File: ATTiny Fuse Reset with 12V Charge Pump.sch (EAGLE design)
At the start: 70 parts, among them IC1 74HC04D, IC2 ATTinyx4, IC3 ATTinyx5/13, M1 MOUNTINGHOLE2.0, M2 MOUNTINGHOLE2.0, Q1 BSS138, Q2 PMV65XP, Q3 BSS138, Q4 BSS138, Q5 BSS138, Q6 BSS138, Q7 BSS138, Q8 BSS130, SW4 SWITCH_SPDT, SW5 SWITCH_SPDT, U1 ARDUINOR3-BPLACE

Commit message: Schematic and board layout improvment
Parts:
- LED1: value green -> pmode
- LED10: value yellow -> H.B.
- LED2: value red -> err
- LED3: value red -> PB5 rst
- LED4: value red -> PB4
- LED5: value red -> PB3
- LED6: value red -> PB2
- LED7: value red -> PB1
- LED8: value red -> PB0
- LED9: value green -> HV on
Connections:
- net N$7: now also A1.PB4; no longer IC1E.I
- net SCI: now also IC1C.I; no longer IC1A.I
- net SDI_MOSI: no longer IC1D.I
- net SII-MISO: now also IC1A.I; no longer IC1C.I

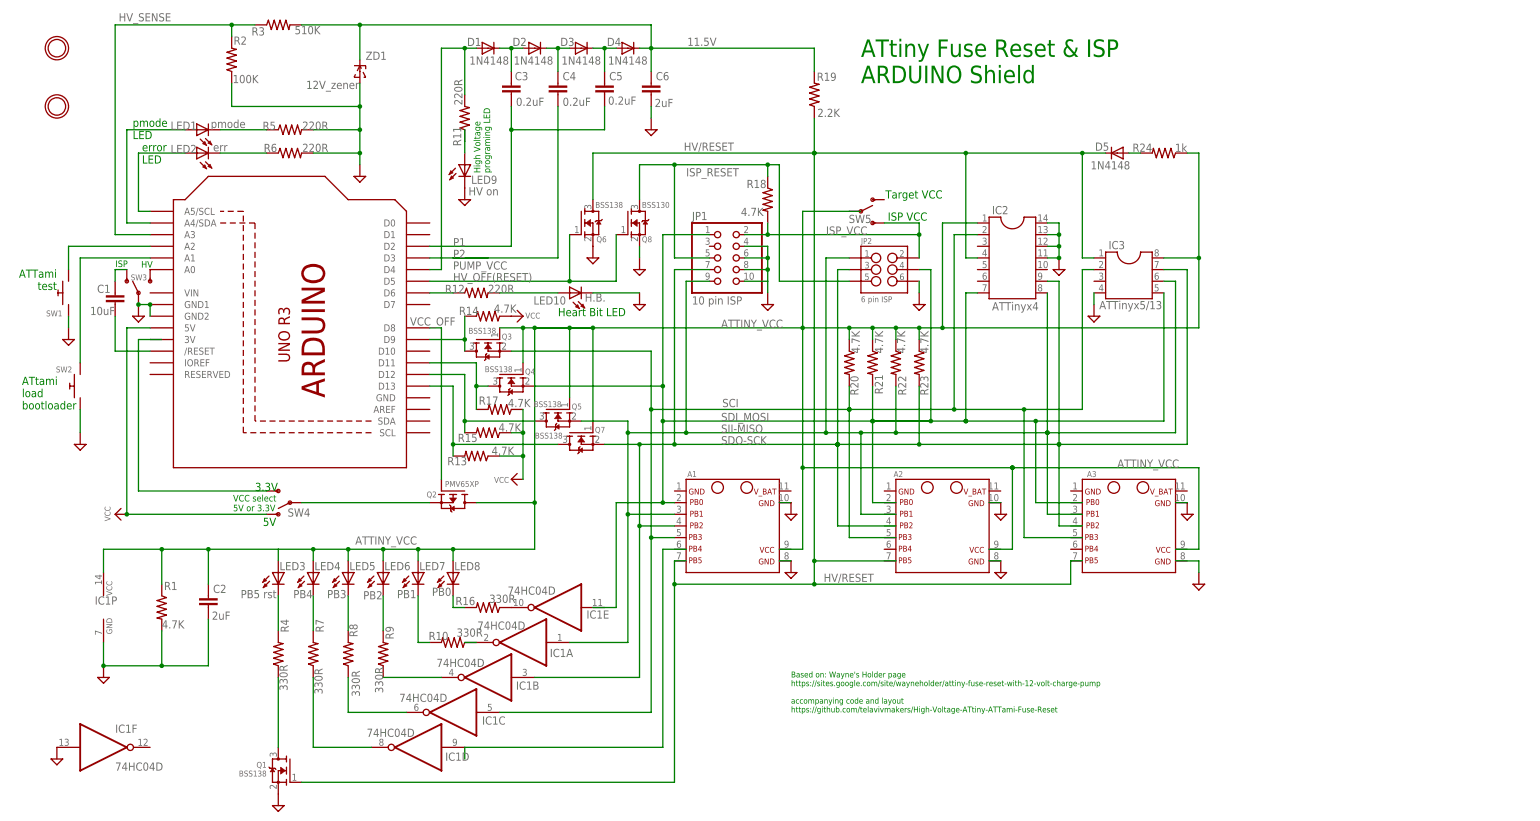
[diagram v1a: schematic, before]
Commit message: "TARGET/ ISP VCC switch"-B-Gone
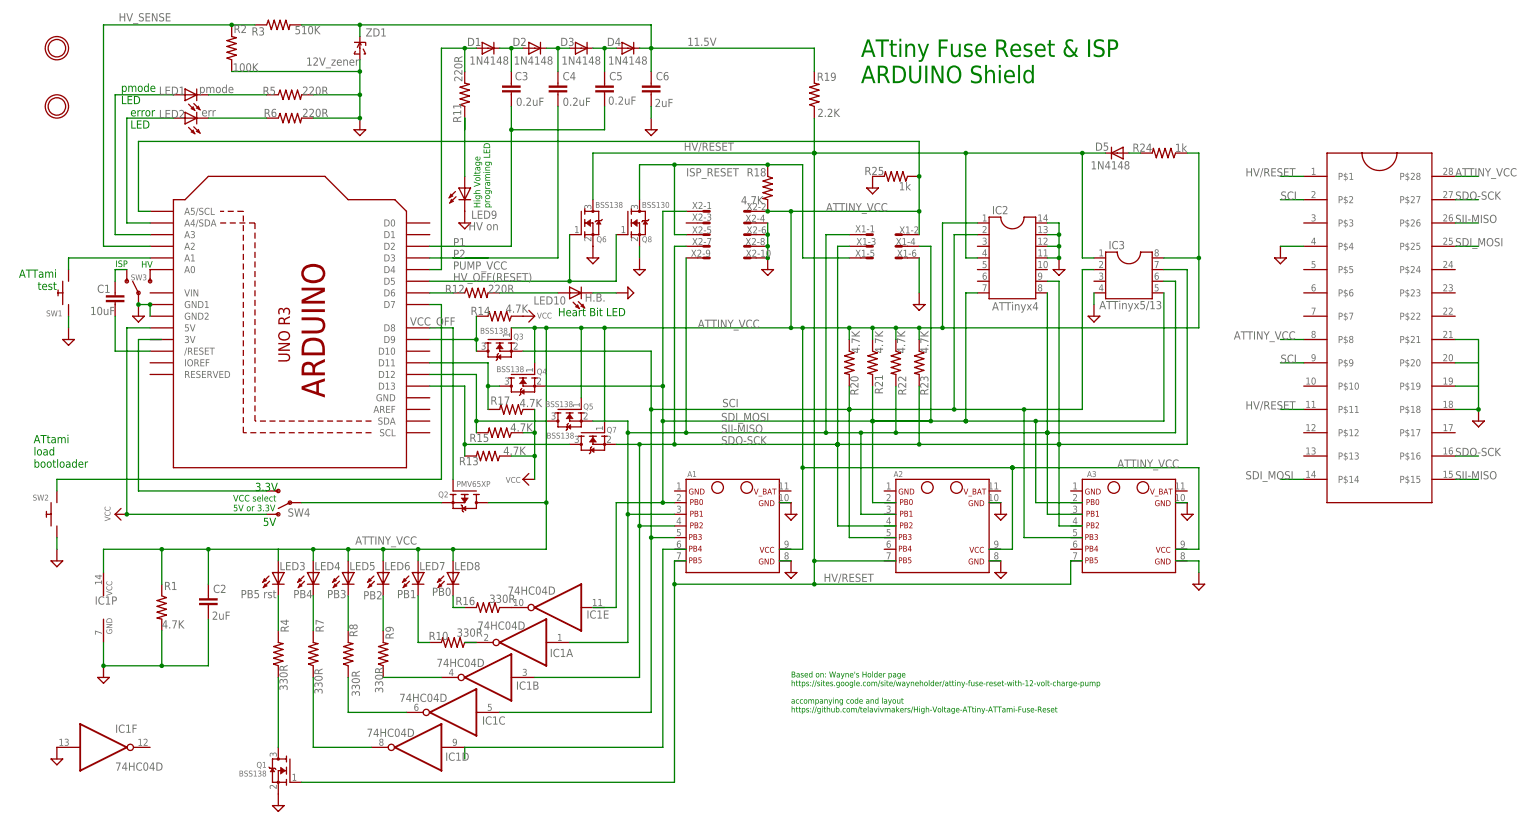
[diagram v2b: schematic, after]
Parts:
- removed JP1: 10 pin ISP, microbuilder:HEADER-2X5
- removed JP2: 6 pin ISP, SparkFun-Connectors:M03X2
- removed SW5: SWITCH_SPDT, SparkFun-Electromechanical:SWITCH_SPDT
- added R25: 1k, ATtami:RESISTOR0805-RES
- added U$1: ZIFSOCKET-28-3ZIFFSOCKET-28-3, SparkFun-Connectors:ZIFSOCKET-28-3ZIFFSOCKET-28-3
- added X1: 057-006-1, con-panduit:057-006-1
- added X2: 057-010-1, con-panduit:057-010-1
- IC2: device gm-ics:DIL14 -> ic-package:DIL14S
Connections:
- removed net ISP_VCC: JP1.2, JP2.2, R18.2, SW5.S
- new net N$50: U$1.P$20
- new net N$51: U$1.P$19
- net ATTINY_VCC: now also R18.2, R25.1, U$1.P$28, U$1.P$8, U1.A5/SCL, X1-2.S, X2-2.S; no longer SW5.P
- net GND: now also R25.2, U$1.P$18, U$1.P$21, U$1.P$4, X1-6.S, X2-10.S, X2-4.S, X2-6.S, X2-8.S; no longer JP1.10, JP1.4, JP1.6, JP1.8, JP2.6
- net HV/RESET: now also U$1.P$1, U$1.P$11
- net HV_SENSE: now also U1.A2; no longer U1.A3
- net ISP_RESET: now also X1-5.S, X2-5.S; no longer JP1.5, JP2.5
- net N$17: now also U1.A4/SDA; no longer U1.A5/SCL
- net N$18: now also U1.A3; no longer U1.A4/SDA
- net N$22: now also U1.D7; no longer U1.A1
- net N$36: now also X1-1.S; no longer JP2.1
- net N$9: now also U1.A1; no longer U1.A2
- net SCI: now also U$1.P$2, U$1.P$9
- net SDI_MOSI: now also U$1.P$14, U$1.P$25, X1-4.S, X2-1.S; no longer JP1.1, JP2.4
- net SDO-SCK: now also U$1.P$16, U$1.P$27, X1-3.S, X2-7.S; no longer JP1.7, JP2.3
- net SII-MISO: now also U$1.P$15, U$1.P$26, X2-9.S; no longer JP1.9
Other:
- note removed: "ISP VCC"
- note removed: "Target VCC"
- moved on the sheet: LED1, LED2, LED9, Q2, Q3, Q4, Q5, Q7, R11, R13, R14, R15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

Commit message: added array resistors, moved transistor under attami
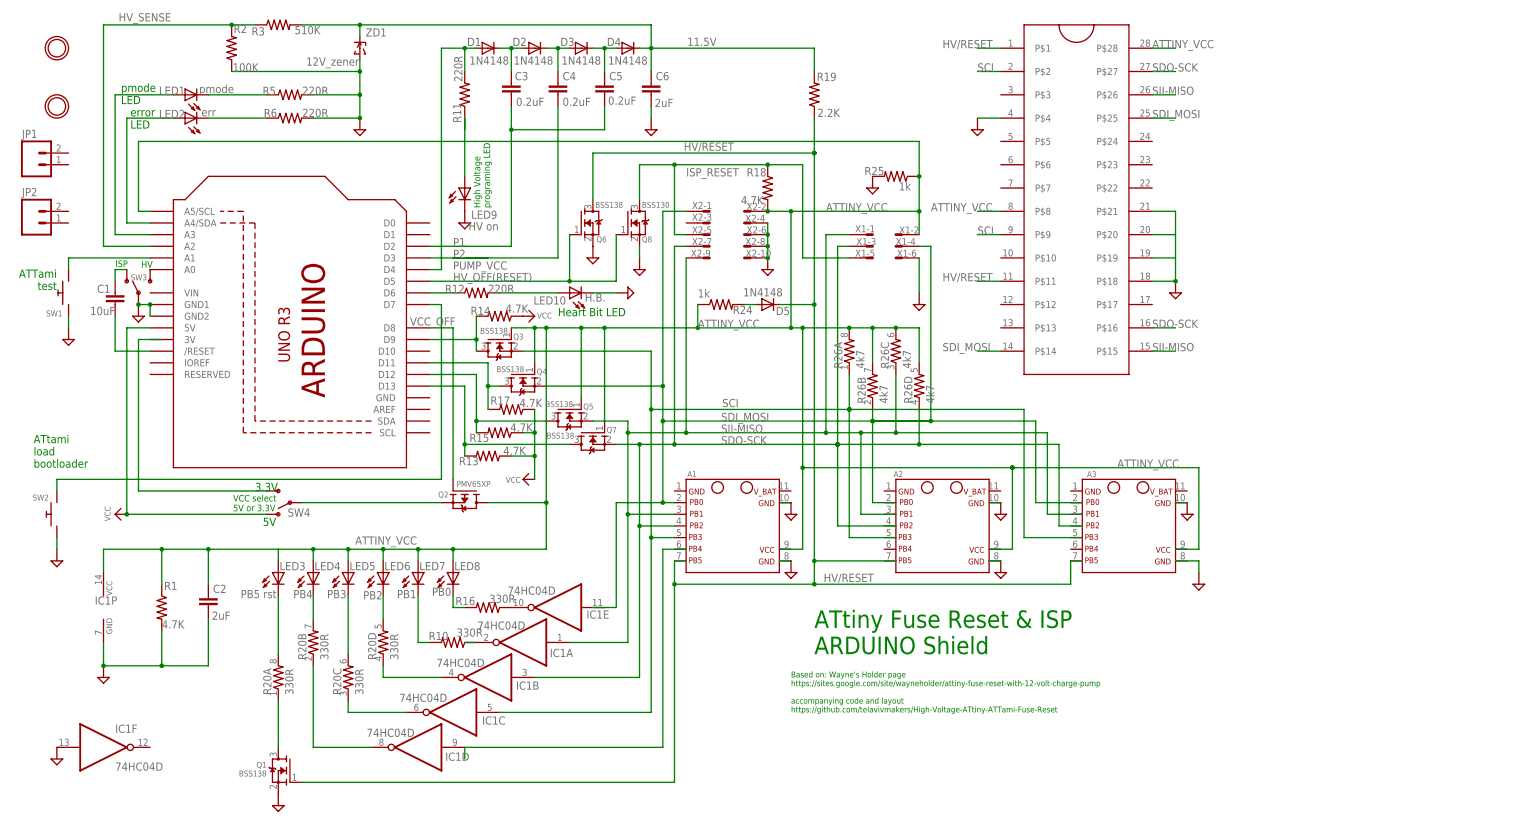
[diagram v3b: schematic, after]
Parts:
- removed IC2: ATTinyx4, ic-package:DIL14S
- removed IC3: ATTinyx5/13, reprap:DIL8S
- removed R21, R22, R23: 4.7K, ATtami:RESISTOR0805-RES
- removed R4, R7, R8, R9: 330R, ATtami:RESISTOR0805-RES
- added JP1, JP2: M02POGO_PIN_HOLES_ONLY, SparkFun-Connectors:M02POGO_PIN_HOLES_ONLY
- added R26: 4k7, SparkFun-Passives:RESISTOR-ARRAY0603-ARV
- R20: value 4.7K -> 330R; device ATtami:RESISTOR0805-RES -> SparkFun-Passives:RESISTOR-ARRAY0603-ARV
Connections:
- net ATTINY_VCC: now also R26A.2, R26B.2, R26C.2, R26D.2; no longer IC2.1, IC3.8, R20.1, R21.1, R22.1, R23.1
- net GND: no longer IC2.11, IC2.12, IC2.13, IC2.14, IC3.4
- net HV/RESET: no longer IC2.4, IC3.1
- net N$23: now also R20B.2; no longer R7.2
- net N$24: now also R20D.1; no longer R9.1
- net N$26: now also R20C.1; no longer R8.1
- net N$28: now also R20B.1; no longer R7.1
- net N$29: now also R20D.2; no longer R9.2
- net N$30: now also R20C.2; no longer R8.2
- net N$35: now also R20A.1; no longer R4.1
- net N$39: now also R20A.2; no longer R4.2
- net SCI: now also R26A.1; no longer IC2.2, IC3.2, R20.2
- net SDI_MOSI: now also R26B.1; no longer IC2.7, IC3.5, R21.2
- net SDO-SCK: now also R26D.1; no longer IC2.9, IC3.7, R23.2
- net SII-MISO: now also R26C.1; no longer IC2.8, IC3.6, R22.2
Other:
- moved on the sheet: D5, R24

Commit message: zif inside, aded to lib, removed 10 pin ISP
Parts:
- removed X2: 057-010-1, con-panduit:057-010-1
- U$1: device SparkFun-Connectors:ZIFSOCKET-28-3ZIFFSOCKET-28-3 -> ATTiny Fuse Reset with 12V Charge Pump:ZIFSOCKET-28-3ZIFFSOCKET-28-3
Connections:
- net ATTINY_VCC: no longer X2-2.S
- net GND: no longer X2-10.S, X2-4.S, X2-6.S, X2-8.S
- net ISP_RESET: no longer X2-5.S
- net SDI_MOSI: no longer X2-1.S
- net SDO-SCK: no longer X2-7.S
- net SII-MISO: no longer X2-9.S
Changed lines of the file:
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@@
 <part name="A3" library="ATtami" deviceset="ATTANI_BREAKOUT_PINS" device=""/>
 <part name="A2" library="ATtami" deviceset="ATTANI_BREAKOUT_PINS" device=""/>
-<part name="SUPPLY13" library="supply2" deviceset="GND" device=""/>
 <part name="C2" library="ATtami" deviceset="CAP" device="0805" value="2uF"/>
 <part name="SUPPLY15" library="supply2" deviceset="GND" device=""/>
@@
 <part name="SUPPLY8" library="supply2" deviceset="GND" device=""/>
 <part name="X1" library="con-panduit" deviceset="057-006-" device="1" value=""/>
-<part name="X2" library="con-panduit" deviceset="057-010-" device="1" value=""/>
-<part name="U$1" library="SparkFun-Connectors" deviceset="ZIFSOCKET-28-3" device="ZIFFSOCKET-28-3"/>
+<part name="U$1" library="ATTiny Fuse Reset with 12V Charge Pump" deviceset="ZIFSOCKET-28-3" device="ZIFFSOCKET-28-3"/>
 <part name="SUPPLY23" library="supply2" deviceset="GND" device=""/>
 <part name="SUPPLY24" library="supply2" deviceset="GND" device=""/>
@@
 <attribute name="NAME" x="-127.508" y="76.708" size="1.27" layer="95"/>
 </instance>
-<instance part="SUPPLY13" gate="GND" x="-154.94" y="121.92" smashed="yes"/>
 <instance part="C2" gate="G$1" x="-276.86" y="48.26" smashed="yes">
 <attribute name="NAME" x="-275.844" y="51.435" size="1.778" layer="95"/>
@@
 <instance part="X1" gate="-6" x="-127" y="124.46" smashed="yes" rot="R180">
 <attribute name="NAME" x="-122.428" y="126.238" size="1.524" layer="95" rot="R180"/>
-</instance>
-<instance part="X2" gate="-1" x="-167.64" y="134.62" smashed="yes">
-<attribute name="NAME" x="-171.45" y="135.128" size="1.524" layer="95"/>
-<attribute name="VALUE" x="-170.18" y="136.525" size="1.778" layer="96"/>
-</instance>
-<instance part="X2" gate="-2" x="-160.02" y="134.62" smashed="yes" rot="R180">
-<attribute name="NAME" x="-155.194" y="136.398" size="1.524" layer="95" rot="R180"/>
-</instance>
-<instance part="X2" gate="-3" x="-167.64" y="132.08" smashed="yes">
-<attribute name="NAME" x="-171.45" y="132.588" size="1.524" layer="95"/>
-</instance>
-<instance part="X2" gate="-4" x="-160.02" y="132.08" smashed="yes" rot="R180">
-<attribute name="NAME" x="-155.448" y="133.858" size="1.524" layer="95" rot="R180"/>
-</instance>
-<instance part="X2" gate="-5" x="-167.64" y="129.54" smashed="yes">
-<attribute name="NAME" x="-171.45" y="129.794" size="1.524" layer="95"/>
-</instance>
-<instance part="X2" gate="-6" x="-160.02" y="129.54" smashed="yes" rot="R180">
-<attribute name="NAME" x="-155.194" y="131.318" size="1.524" layer="95" rot="R180"/>
-</instance>
-<instance part="X2" gate="-7" x="-167.64" y="127" smashed="yes">
-<attribute name="NAME" x="-171.45" y="127.254" size="1.524" layer="95"/>
-</instance>
-<instance part="X2" gate="-8" x="-160.02" y="127" smashed="yes" rot="R180">
-<attribute name="NAME" x="-155.448" y="128.778" size="1.524" layer="95" rot="R180"/>
-</instance>
-<instance part="X2" gate="-9" x="-167.64" y="124.46" smashed="yes">
-<attribute name="NAME" x="-171.704" y="124.714" size="1.524" layer="95"/>
-</instance>
-<instance part="X2" gate="-10" x="-160.02" y="124.46" smashed="yes" rot="R180">
-<attribute name="NAME" x="-154.178" y="126.238" size="1.524" layer="95" rot="R180"/>
 </instance>
 <instance part="U$1" gate="G$1" x="-99.06" y="99.06" smashed="yes"/>
@@
 <wire x1="-292.1" y1="134.62" x2="-292.1" y2="149.86" width="0.1524" layer="91"/>
 <pinref part="R18" gate="G$1" pin="2"/>
-<pinref part="X2" gate="-2" pin="S"/>
-<junction x="-154.94" y="134.62"/>
 <wire x1="-149.86" y1="134.62" x2="-154.94" y2="134.62" width="0.1524" layer="91"/>
 <wire x1="-149.86" y1="134.62" x2="-149.86" y2="109.22" width="0.1524" layer="91"/>
@@
 <pinref part="SUPPLY16" gate="GND" pin="GND"/>
 <pinref part="X1" gate="-6" pin="S"/>
-</segment>
-<segment>
-<wire x1="-154.94" y1="132.08" x2="-154.94" y2="129.54" width="0.1524" layer="91"/>
-<pinref part="SUPPLY13" gate="GND" pin="GND"/>
-<pinref part="X2" gate="-4" pin="S"/>
-<pinref part="X2" gate="-6" pin="S"/>
-<wire x1="-154.94" y1="129.54" x2="-154.94" y2="127" width="0.1524" layer="91"/>
-<junction x="-154.94" y="129.54"/>
-<pinref part="X2" gate="-8" pin="S"/>
-<wire x1="-154.94" y1="127" x2="-154.94" y2="124.46" width="0.1524" layer="91"/>
-<junction x="-154.94" y="127"/>
-<pinref part="X2" gate="-10" pin="S"/>
-<junction x="-154.94" y="124.46"/>
 </segment>
 <segment>
@@
 <segment>
 <label x="-165.1" y="86.36" size="1.778" layer="95"/>
-<wire x1="-172.72" y1="124.46" x2="-172.72" y2="86.36" width="0.1524" layer="91"/>
-<wire x1="-185.42" y1="86.36" x2="-172.72" y2="86.36" width="0.1524" layer="91"/>
-<wire x1="-172.72" y1="86.36" x2="-134.62" y2="86.36" width="0.1524" layer="91"/>
-<junction x="-172.72" y="86.36"/>
+<wire x1="-185.42" y1="86.36" x2="-134.62" y2="86.36" width="0.1524" layer="91"/>
 <wire x1="-134.62" y1="86.36" x2="-127" y2="86.36" width="0.1524" layer="91"/>
 <wire x1="-127" y1="86.36" x2="-93.98" y2="86.36" width="0.1524" layer="91"/>
@@
 <wire x1="-185.42" y1="40.64" x2="-185.42" y2="68.58" width="0.1524" layer="91"/>
 <junction x="-185.42" y="68.58"/>
-<pinref part="X2" gate="-9" pin="S"/>
 <pinref part="R26" gate="C" pin="1"/>
 </segment>
@@
 <net name="SDO-SCK" class="0">
 <segment>
-<wire x1="-175.26" y1="83.82" x2="-175.26" y2="127" width="0.1524" layer="91"/>
 <label x="-165.1" y="83.82" size="1.778" layer="95"/>
-<wire x1="-182.88" y1="83.82" x2="-175.26" y2="83.82" width="0.1524" layer="91"/>
-<wire x1="-175.26" y1="83.82" x2="-139.7" y2="83.82" width="0.1524" layer="91"/>
-<junction x="-175.26" y="83.82"/>
+<wire x1="-182.88" y1="83.82" x2="-139.7" y2="83.82" width="0.1524" layer="91"/>
 <wire x1="-139.7" y1="83.82" x2="-121.92" y2="83.82" width="0.1524" layer="91"/>
 <wire x1="-121.92" y1="83.82" x2="-91.44" y2="83.82" width="0.1524" layer="91"/>
@@
 <junction x="-182.88" y="66.04"/>
 <pinref part="X1" gate="-3" pin="S"/>
-<pinref part="X2" gate="-7" pin="S"/>
-<wire x1="-175.26" y1="127" x2="-172.72" y2="127" width="0.1524" layer="91"/>
 <pinref part="R26" gate="D" pin="1"/>
 </segment>
@@
 <wire x1="-132.08" y1="88.9" x2="-96.52" y2="88.9" width="0.1524" layer="91"/>
 <label x="-165.1" y="88.9" size="1.778" layer="95"/>
-<wire x1="-177.8" y1="134.62" x2="-177.8" y2="96.52" width="0.1524" layer="91"/>
 <wire x1="-177.8" y1="96.52" x2="-177.8" y2="88.9" width="0.1524" layer="91"/>
 <wire x1="-121.92" y1="127" x2="-119.38" y2="127" width="0.1524" layer="91"/>
@@
 <pinref part="Q4" gate="G$1" pin="S"/>
 <wire x1="-203.2" y1="96.52" x2="-177.8" y2="96.52" width="0.1524" layer="91"/>
-<junction x="-177.8" y="96.52"/>
 <wire x1="-177.8" y1="88.9" x2="-177.8" y2="71.12" width="0.1524" layer="91"/>
 <junction x="-177.8" y="88.9"/>
@@
 <junction x="-177.8" y="71.12"/>
 <pinref part="X1" gate="-4" pin="S"/>
-<pinref part="X2" gate="-1" pin="S"/>
-<wire x1="-177.8" y1="134.62" x2="-172.72" y2="134.62" width="0.1524" layer="91"/>
 <pinref part="R26" gate="B" pin="1"/>
 </segment>
@@
 <pinref part="Q8" gate="G$1" pin="D"/>
 <wire x1="-182.88" y1="144.78" x2="-182.88" y2="137.16" width="0.1524" layer="91"/>
-<wire x1="-175.26" y1="144.78" x2="-182.88" y2="144.78" width="0.1524" layer="91"/>
-<junction x="-175.26" y="144.78"/>
-<wire x1="-175.26" y1="144.78" x2="-175.26" y2="129.54" width="0.1524" layer="91"/>
-<wire x1="-154.94" y1="144.78" x2="-175.26" y2="144.78" width="0.1524" layer="91"/>
+<wire x1="-154.94" y1="144.78" x2="-182.88" y2="144.78" width="0.1524" layer="91"/>
 <pinref part="R18" gate="G$1" pin="1"/>
 <junction x="-154.94" y="144.78"/>
@@
 <label x="-172.72" y="142.24" size="1.778" layer="95"/>
 <pinref part="X1" gate="-5" pin="S"/>
-<pinref part="X2" gate="-5" pin="S"/>
-<wire x1="-175.26" y1="129.54" x2="-172.72" y2="129.54" width="0.1524" layer="91"/>
-</segment>
-</net>
+</segment>
+</net>
